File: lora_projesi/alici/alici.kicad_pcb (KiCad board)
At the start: 4 copper layers, 88 x 102 mm, 127 parts, among them J1 USB-C, J2 SMA, J3 RJ45, J4 u.FL (ANA ANTEN), J5 12 V GIRIS, J6 LAMBA, J7 MICRO-SIM, J8 u.FL (YARDIMCI ANTEN, ISTEGE 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, K1 SRD-12VDC-SL-A, Q1 AO3401A, Q2 MMBT2222A, Q3 MMBT2222A, Q4 MMBT2222A, SW1 DUGME, U1 ESP32-S3-WROOM-1-N4, U10 SIM7600SA, U11 AP2112K-3.3, U12 ESDA6V1-5SC6, U4 RFM95W-915S2, U5 TPS62933DRLR, U6 TPS62933DRLR, U7 USBLC6-2SC6, U8 TXB0104PW, U9 W5500, Y1 25 MHz

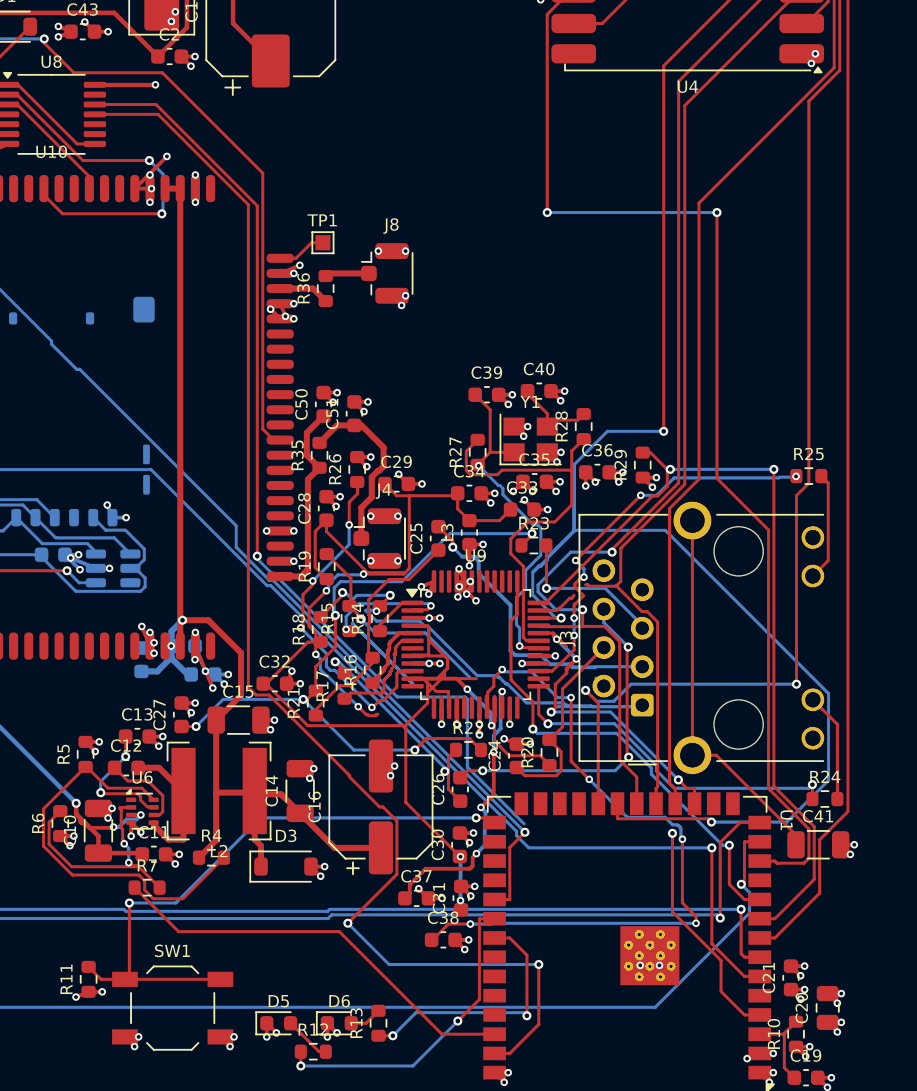
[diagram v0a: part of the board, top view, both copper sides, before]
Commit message: Alici: 5 baglantisiz, 0 DRC hatasi; bosluk kapatici
Co-Authored-By: Claude Sonnet 5.5 <noreply@anthropic.com>
Claude-Session: https://claude.ai/code/session_01Q71gHQtKJ86ZE2CtYTYSwP
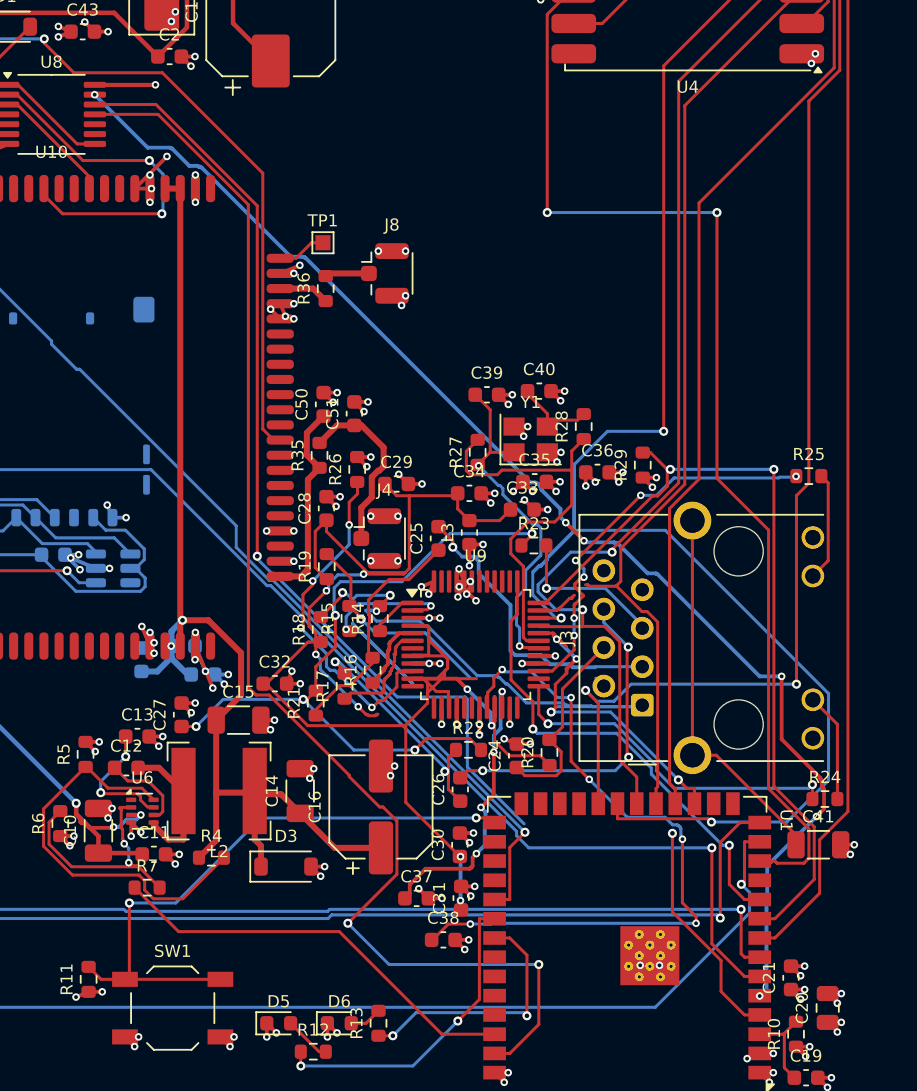
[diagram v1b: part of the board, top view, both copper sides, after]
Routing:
- net MODEM_RXD_H: track 0.00 -> 85.7 mm, vias 0 -> 6
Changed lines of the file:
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@@
   (segment (start 32.9121 79.6117) (end 32.7805 79.4801) (width 0.2) (layer "B.Cu") (net 43))
   (segment (start 32.7805 79.4801) (end 5.6108 79.4801) (width 0.2) (layer "B.Cu") (net 43))
+  (segment (start 78.75 70.8) (end 78.75 70.85) (width 0.25) (layer "F.Cu") (net 44))
+  (segment (start 78.75 70.85) (end 78.8 70.9) (width 0.25) (layer "F.Cu") (net 44))
+  (segment (start 79 71.55) (end 79 72.85) (width 0.25) (layer "F.Cu") (net 44))
+  (segment (start 78.85 71.35) (end 78.95 71.45) (width 0.25) (layer "F.Cu") (net 44))
+  (segment (start 76.2 64.1) (end 76.2 68.25) (width 0.25) (layer "F.Cu") (net 44))
+  (segment (start 78.95 71.45) (end 78.95 71.5) (width 0.25) (layer "F.Cu") (net 44))
+  (segment (start 78.8 70.9) (end 78.8 70.95) (width 0.25) (layer "F.Cu") (net 44))
+  (segment (start 76.2 68.25) (end 78.75 70.8) (width 0.25) (layer "F.Cu") (net 44))
+  (segment (start 78.95 71.5) (end 79 71.55) (width 0.25) (layer "F.Cu") (net 44))
+  (segment (start 61.95 53.95) (end 63.15 55.15) (width 0.25) (layer "F.Cu") (net 44))
+  (segment (start 78.85 71) (end 78.85 71.35) (width 0.25) (layer "F.Cu") (net 44))
+  (segment (start 78.8 70.95) (end 78.85 71) (width 0.25) (layer "F.Cu") (net 44))
+  (segment (start 79 72.85) (end 78.5 73.35) (width 0.25) (layer "F.Cu") (net 44))
+  (via (at 78.5 73.35) (size 0.5) (drill 0.25) (layers "F.Cu" "B.Cu") (net 44))
+  (via (at 76.2 64.1) (size 0.5) (drill 0.25) (layers "F.Cu" "B.Cu") (net 44))
+  (via (at 30.85 25.7) (size 0.5) (drill 0.25) (layers "F.Cu" "B.Cu") (net 44))
+  (via (at 61.95 53.95) (size 0.5) (drill 0.25) (layers "F.Cu" "B.Cu") (net 44))
+  (via (at 74.75 85.2) (size 0.5) (drill 0.25) (layers "F.Cu" "B.Cu") (net 44))
+  (via (at 63.15 55.15) (size 0.5) (drill 0.25) (layers "F.Cu" "B.Cu") (net 44))
+  (segment (start 60.3 51.65) (end 60.35 51.7) (width 0.25) (layer "B.Cu") (net 44))
+  (segment (start 35.85 29.2) (end 35.9 29.25) (width 0.25) (layer "B.Cu") (net 44))
+  (segment (start 65.35 55.35) (end 65.4 55.35) (width 0.25) (layer "B.Cu") (net 44))
+  (segment (start 60.35 51.8) (end 61.6 53.05) (width 0.25) (layer "B.Cu") (net 44))
+  (segment (start 37.8 30.45) (end 37.85 30.5) (width 0.25) (layer "B.Cu") (net 44))
+  (segment (start 60.25 51.5) (end 60.25 51.55) (width 0.25) (layer "B.Cu") (net 44))
+  (segment (start 67.9 57.3) (end 67.95 57.35) (width 0.25) (layer "B.Cu") (net 44))
+  (segment (start 60.3 51.6) (end 60.3 51.65) (width 0.25) (layer "B.Cu") (net 44))
+  (segment (start 65.15 55.25) (end 65.2 55.3) (width 0.25) (layer "B.Cu") (net 44))
+  (segment (start 37.85 30.5) (end 37.9 30.5) (width 0.25) (layer "B.Cu") (net 44))
+  (segment (start 30.85 25.7) (end 34.35 29.2) (width 0.25) (layer "B.Cu") (net 44))
+  (segment (start 75.2 79.05) (end 75.2 84.75) (width 0.25) (layer "B.Cu") (net 44))
+  (segment (start 44.65 36.4) (end 44.7 36.45) (width 0.25) (layer "B.Cu") (net 44))
+  (segment (start 60.25 51.55) (end 60.3 51.6) (width 0.25) (layer "B.Cu") (net 44))
+  (segment (start 67.35 57.3) (end 67.9 57.3) (width 0.25) (layer "B.Cu") (net 44))
+  (segment (start 75.25 76.6) (end 75.25 79) (width 0.25) (layer "B.Cu") (net 44))
+  (segment (start 61.6 53.05) (end 61.6 53.6) (width 0.25) (layer "B.Cu") (net 44))
+  (segment (start 35.95 29.25) (end 37.1 30.4) (width 0.25) (layer "B.Cu") (net 44))
+  (segment (start 65.4 55.35) (end 67.35 57.3) (width 0.25) (layer "B.Cu") (net 44))
+  (segment (start 60.1 51.4) (end 60.15 51.4) (width 0.25) (layer "B.Cu") (net 44))
+  (segment (start 43.8 36.4) (end 44.65 36.4) (width 0.25) (layer "B.Cu") (net 44))
+  (segment (start 60.35 51.7) (end 60.35 51.8) (width 0.25) (layer "B.Cu") (net 44))
+  (segment (start 59.95 51.3) (end 60 51.35) (width 0.25) (layer "B.Cu") (net 44))
+  (segment (start 37.7 30.45) (end 37.8 30.45) (width 0.25) (layer "B.Cu") (net 44))
+  (segment (start 37.9 30.5) (end 43.8 36.4) (width 0.25) (layer "B.Cu") (net 44))
+  (segment (start 63.25 55.25) (end 65.15 55.25) (width 0.25) (layer "B.Cu") (net 44))
+  (segment (start 60 51.35) (end 60.05 51.35) (width 0.25) (layer "B.Cu") (net 44))
+  (segment (start 74.75 64.1) (end 76.2 64.1) (width 0.25) (layer "B.Cu") (net 44))
+  (segment (start 37.1 30.4) (end 37.65 30.4) (width 0.25) (layer "B.Cu") (net 44))
+  (segment (start 75.25 79) (end 75.2 79.05) (width 0.25) (layer "B.Cu") (net 44))
+  (segment (start 44.7 36.45) (end 44.75 36.45) (width 0.25) (layer "B.Cu") (net 44))
+  (segment (start 59.6 51.3) (end 59.95 51.3) (width 0.25) (layer "B.Cu") (net 44))
+  (segment (start 68 57.35) (end 74.75 64.1) (width 0.25) (layer "B.Cu") (net 44))
+  (segment (start 61.6 53.6) (end 61.95 53.95) (width 0.25) (layer "B.Cu") (net 44))
+  (segment (start 35.9 29.25) (end 35.95 29.25) (width 0.25) (layer "B.Cu") (net 44))
+  (segment (start 34.35 29.2) (end 35.85 29.2) (width 0.25) (layer "B.Cu") (net 44))
+  (segment (start 63.15 55.15) (end 63.25 55.25) (width 0.25) (layer "B.Cu") (net 44))
+  (segment (start 65.2 55.3) (end 65.3 55.3) (width 0.25) (layer "B.Cu") (net 44))
+  (segment (start 60.05 51.35) (end 60.1 51.4) (width 0.25) (layer "B.Cu") (net 44))
+  (segment (start 37.65 30.4) (end 37.7 30.45) (width 0.25) (layer "B.Cu") (net 44))
+  (segment (start 44.75 36.45) (end 59.6 51.3) (width 0.25) (layer "B.Cu") (net 44))
+  (segment (start 65.3 55.3) (end 65.35 55.35) (width 0.25) (layer "B.Cu") (net 44))
+  (segment (start 78.5 73.35) (end 75.25 76.6) (width 0.25) (layer "B.Cu") (net 44))
+  (segment (start 60.15 51.4) (end 60.25 51.5) (width 0.25) (layer "B.Cu") (net 44))
+  (segment (start 67.95 57.35) (end 68 57.35) (width 0.25) (layer "B.Cu") (net 44))
+  (segment (start 75.2 84.75) (end 74.75 85.2) (width 0.25) (layer "B.Cu") (net 44))
   (segment (start 41.5024 65.331) (end 42.3592 65.331) (width 0.2) (layer "F.Cu") (net 45))
   (segment (start 49.6598 72.7201) (end 49.8783 72.7201) (width 0.2) (layer "F.Cu") (net 45))
@@
   (segment (start 77.2277 19) (end 77.525 19) (width 0.2) (layer "F.Cu") (net 66))
   (segment (start 65.5832 55.6426) (end 69.8049 51.4209) (width 0.2) (layer "F.Cu") (net 66))
+  (segment (start 62.5 58.75) (end 62.3 58.95) (width 0.2) (layer "F.Cu") (net 66))
   (segment (start 61.365 59.75) (end 60.1625 59.75) (width 0.2) (layer "F.Cu") (net 66))
   (segment (start 63.25 58.05) (end 63.4 58.05) (width 0.2) (layer "F.Cu") (net 66))
@@
   (segment (start 61.5 63.3) (end 61.55 63.3) (width 0.2) (layer "F.Cu") (net 84))
   (segment (start 61.05 63.75) (end 61.5 63.3) (width 0.2) (layer "F.Cu") (net 84))
+  (segment (start 62.55 58) (end 62.6 57.95) (width 0.2) (layer "F.Cu") (net 84))
+  (segment (start 62.55 59.35) (end 62.55 59.3) (width 0.2) (layer "F.Cu") (net 84))
+  (segment (start 62.55 58.2) (end 63.1 58.75) (width 0.2) (layer "F.Cu") (net 84))
   (segment (start 63.1 58.75) (end 63.1 58.8) (width 0.2) (layer "F.Cu") (net 84))
-  (segment (start 62.55 58) (end 62.6 57.95) (width 0.2) (layer "F.Cu") (net 84))
-  (segment (start 62.55 58.2) (end 63.1 58.75) (width 0.2) (layer "F.Cu") (net 84))
-  (segment (start 62.55 59.35) (end 62.55 59.3) (width 0.2) (layer "F.Cu") (net 84))
   (segment (start 60.15 63.75) (end 61.05 63.75) (width 0.2) (layer "F.Cu") (net 84))
   (segment (start 62.5 62.35) (end 62.5 61.4) (width 0.2) (layer "F.Cu") (net 84))
   (segment (start 63 57.7) (end 63.15 57.55) (width 0.2) (layer "F.Cu") (net 84))
   (segment (start 62.5 59.4) (end 62.55 59.35) (width 0.2) (layer "F.Cu") (net 84))
-  (segment (start 62.55 58) (end 62.55 58.2) (width 0.2) (layer "F.Cu") (net 84))
   (segment (start 61.55 63.3) (end 62.5 62.35) (width 0.2) (layer "F.Cu") (net 84))
   (segment (start 62.5 60.25) (end 62.5 59.4) (width 0.2) (layer "F.Cu") (net 84))
@@
   (segment (start 62.85 57.7) (end 63 57.7) (width 0.2) (layer "F.Cu") (net 84))
   (segment (start 62.6 56.45) (end 66.9 52.15) (width 0.2) (layer "F.Cu") (net 84))
+  (segment (start 62.55 58) (end 62.55 58.2) (width 0.2) (layer "F.Cu") (net 84))
   (via (at 66.9 52.15) (size 0.5) (drill 0.25) (layers "F.Cu" "B.Cu") (net 84))
   (via (at 62.5 61.4) (size 0.5) (drill 0.25) (layers "F.Cu" "B.Cu") (net 84))

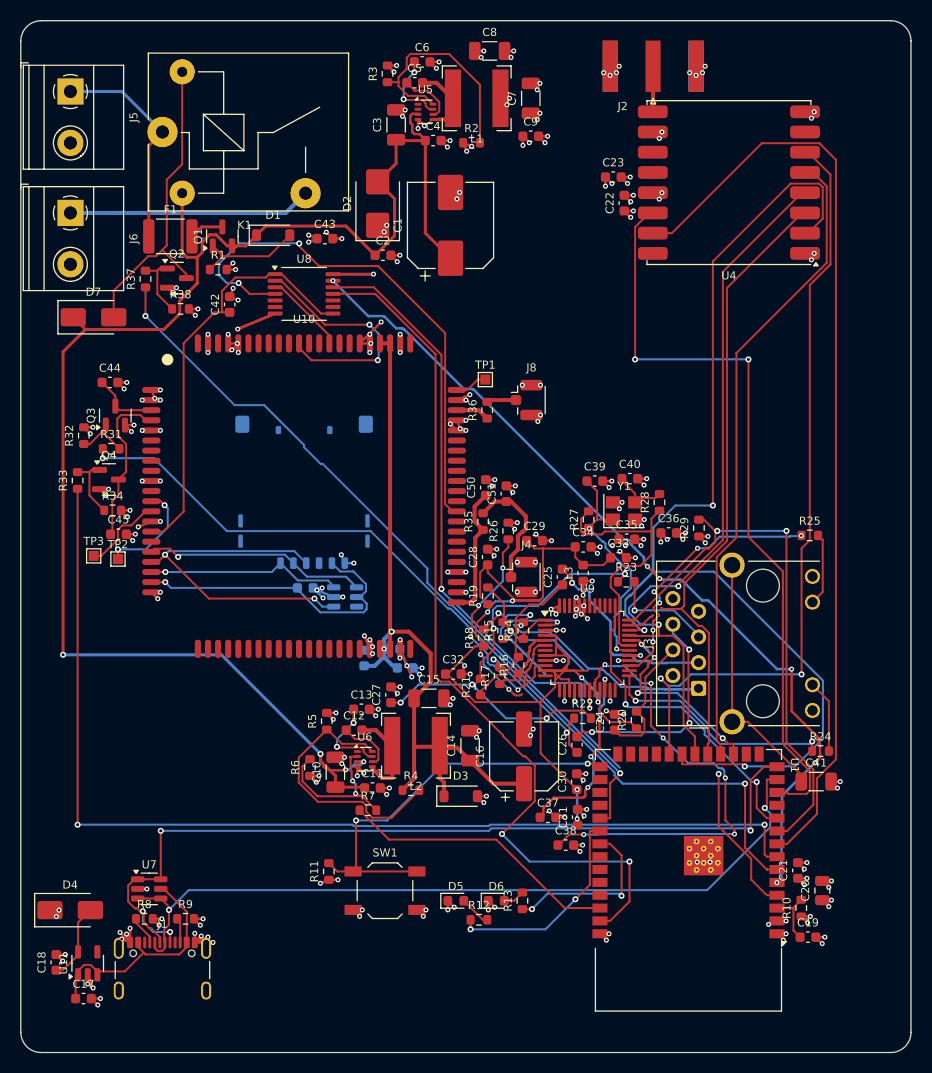
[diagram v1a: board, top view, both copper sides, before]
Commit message: Alici: 2 baglantisiz kaldi (son gecis suruyor)
Co-Authored-By: Claude Sonnet 5.5 <noreply@anthropic.com>
Claude-Session: https://claude.ai/code/session_01Q71gHQtKJ86ZE2CtYTYSwP
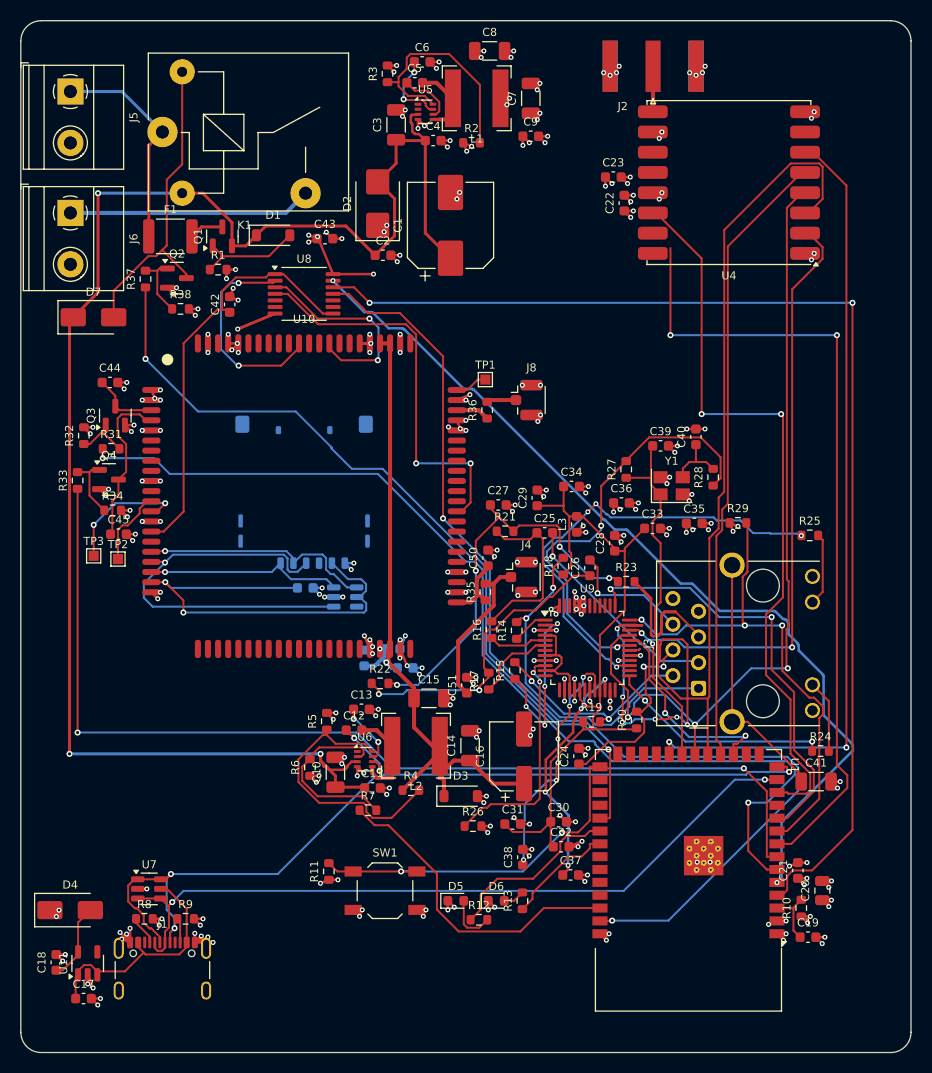
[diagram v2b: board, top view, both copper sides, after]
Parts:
- moved R26 29.4 mm to (44.7, 79.6), turned to 0 degrees
- moved C27 21.6 mm to (47.2, 47.9), turned to 0 degrees
- moved R22 20.3 mm to (35.5, 65.5)
- moved C32 20.1 mm to (53.4, 81.7)
- moved C51 19.3 mm to (44.1, 65.7)
- moved C26 17.5 mm to (56.3, 54.1)
- moved R19 16.1 mm to (56.4, 69.3), turned to 0 degrees
- moved R21 15.6 mm to (47.9, 50.5), turned to 0 degrees
- moved C28 12.6 mm to (58.7, 51.7)
- moved R18 10.6 mm to (53.6, 53.9)
- moved C40 7.74 mm to (66.7, 41.1), turned to 90 degrees
- moved C39 7.37 mm to (63.2, 42.0)
- moved R35 6.97 mm to (45.9, 56.5)
- moved C50 6.97 mm to (46.2, 53.1)
- moved C35 6.85 mm to (66.6, 49.7)
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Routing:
- net SPI_MOSI: track 65.4 -> 114.9 mm, vias 0 -> 6
- net SPI_MISO: track 111.8 -> 72.6 mm
- net +3V3A: track 116.7 -> 80.8 mm, vias 8 -> 0
- net MODEM_TXD_H: track 79.2 -> 115.1 mm
- net TOCAP: track 46.2 -> 24.3 mm
- net MODEM_STATUS: track 87.5 -> 107.1 mm
- net W_ACTLED: track 26.8 -> 44.8 mm, vias 6 -> 4
- net XO: track 27.1 -> 42.9 mm, vias 0 -> 2
- net RX_B: track 15.6 -> 30.4 mm
- net USIM_VDD: track 30.3 -> 44.2 mm, vias 1 -> 2
- net LORA_DIO1: track 93.1 -> 79.5 mm, vias 0 -> 2
- net M_STATUS: track 52.8 -> 39.3 mm
- net MODEM_PWRKEY_CTL: track 88.3 -> 101.8 mm
- net M_RXD: track 8.12 -> 20.9 mm, vias 0 -> 2
- net ETH_RST: track 31.9 -> 42.7 mm
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
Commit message: izgara: adim adim surec dongusu
Co-Authored-By: Claude Sonnet 5.5 <noreply@anthropic.com>
Claude-Session: https://claude.ai/code/session_01Q71gHQtKJ86ZE2CtYTYSwP
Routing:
- net RCT: track 21.1 -> 16.7 mm
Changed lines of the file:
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@@
   (segment (start 76.3781 89.9365) (end 76.3781 87.7731) (width 0.2) (layer "F.Cu") (net 19))
   (segment (start 76.325 87.72) (end 77.15 86.895) (width 0.2) (layer "F.Cu") (net 19))
-  (segment (start 61.75 61.95) (end 61.2 61.4) (width 0.2) (layer "F.Cu") (net 20))
-  (segment (start 61.2 61.4) (end 61.15 61.4) (width 0.2) (layer "F.Cu") (net 20))
+  (segment (start 61.75 61.95) (end 61.75 62) (width 0.2) (layer "F.Cu") (net 20))
   (segment (start 61.15 61.4) (end 61.05 61.3) (width 0.2) (layer "F.Cu") (net 20))
   (segment (start 61 61.25) (end 61.05 61.3) (width 0.2) (layer "F.Cu") (net 20))
@@
   (segment (start 60.1625 61.25) (end 61.0447 61.25) (width 0.2) (layer "F.Cu") (net 20))
   (segment (start 62.1241 62.3294) (end 62.1241 65.1352) (width 0.2) (layer "F.Cu") (net 20))
-  (segment (start 61.75 62) (end 61.75 61.95) (width 0.2) (layer "F.Cu") (net 20))
+  (segment (start 61.2 61.4) (end 61.75 61.95) (width 0.2) (layer "F.Cu") (net 20))
+  (segment (start 61.15 61.4) (end 61.2 61.4) (width 0.2) (layer "F.Cu") (net 20))
   (segment (start 61.05 61.3) (end 61.1 61.3) (width 0.2) (layer "F.Cu") (net 20))
   (segment (start 62.1241 65.1352) (end 63.6935 66.7046) (width 0.2) (layer "F.Cu") (net 20))
@@
   (segment (start 63.35 59.75) (end 63.35 58.75) (width 0.25) (layer "F.Cu") (net 56))
   (segment (start 67 60.7082) (end 64.6818 58.39) (width 0.2) (layer "F.Cu") (net 56))
-  (segment (start 62.3 60.65) (end 62.35 60.7) (width 0.25) (layer "F.Cu") (net 56))
   (segment (start 63.35 58.75) (end 63.4 58.7) (width 0.25) (layer "F.Cu") (net 56))
-  (segment (start 62.9 60.85) (end 62.95 60.8) (width 0.25) (layer "F.Cu") (net 56))
-  (segment (start 62.45 60.8) (end 62.5 60.85) (width 0.25) (layer "F.Cu") (net 56))
   (segment (start 63.6 58.45) (end 64.65 58.45) (width 0.25) (layer "F.Cu") (net 56))
   (segment (start 63.4 58.65) (end 63.6 58.45) (width 0.25) (layer "F.Cu") (net 56))
@@
   (segment (start 63 60.8) (end 63.3 60.5) (width 0.25) (layer "F.Cu") (net 56))
   (segment (start 63.6 58.45) (end 64.65 58.45) (width 0.25) (layer "F.Cu") (net 56))
-  (segment (start 62.35 60.75) (end 62.4 60.8) (width 0.25) (layer "F.Cu") (net 56))
-  (segment (start 62.95 60.8) (end 63 60.8) (width 0.25) (layer "F.Cu") (net 56))
   (segment (start 63.3 59.8) (end 63.35 59.75) (width 0.25) (layer "F.Cu") (net 56))
   (segment (start 63.35 59.75) (end 63.35 58.75) (width 0.25) (layer "F.Cu") (net 56))
@@
   (segment (start 63.3 60.5) (end 63.3 59.8) (width 0.25) (layer "F.Cu") (net 56))
   (segment (start 64.65 58.45) (end 64.7 58.4) (width 0.25) (layer "F.Cu") (net 56))
-  (segment (start 62.5 60.85) (end 62.9 60.85) (width 0.25) (layer "F.Cu") (net 56))
-  (segment (start 62.4 60.8) (end 62.45 60.8) (width 0.25) (layer "F.Cu") (net 56))
   (segment (start 63 60.8) (end 63.3 60.5) (width 0.25) (layer "F.Cu") (net 56))
-  (segment (start 62.3 57.1) (end 62.3 60.65) (width 0.25) (layer "F.Cu") (net 56))
-  (segment (start 62.35 60.7) (end 62.35 60.75) (width 0.25) (layer "F.Cu") (net 56))
   (segment (start 64.6818 58.39) (end 63.6025 58.39) (width 0.2) (layer "F.Cu") (net 56))
   (segment (start 63.3 60.5) (end 63.3 59.8) (width 0.25) (layer "F.Cu") (net 56))
@@
   (segment (start 61.1 62.2) (end 61.2 62.1) (width 0.2) (layer "F.Cu") (net 91))
   (segment (start 62.2888 42.2045) (end 62.4655 42.0278) (width 0.2) (layer "F.Cu") (net 91))
+  (segment (start 61.1 62.2) (end 61.2 62.1) (width 0.2) (layer "F.Cu") (net 91))
   (segment (start 63.25 48.7) (end 63.25 46.85) (width 0.2) (layer "F.Cu") (net 91))
   (segment (start 62.2888 45.1841) (end 62.2888 42.2045) (width 0.2) (layer "F.Cu") (net 91))
